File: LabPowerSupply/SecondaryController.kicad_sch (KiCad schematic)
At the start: 18 parts, among them Y2 8M

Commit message: Made oscillator caps smd
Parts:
- C1_Y2, C2_Y2: footprint Capacitor_THT:C_Disc_D5.0mm_W2.5mm_P2.50mm -> (none)
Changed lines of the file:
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@@
     (property "Reference" "C2_Y2" (id 0) (at 73.66 91.44 90))
     (property "Value" "100n" (id 1) (at 73.66 93.98 90))
-    (property "Footprint" "Capacitor_THT:C_Disc_D5.0mm_W2.5mm_P2.50mm" (id 2) (at 77.47 87.3252 0)
+    (property "Footprint" "" (id 2) (at 77.47 87.3252 0)
       (effects (font (size 1.27 1.27)) hide)
     )
@@
     (property "Reference" "C1_Y2" (id 0) (at 73.66 72.39 90))
     (property "Value" "100n" (id 1) (at 73.66 74.93 90))
-    (property "Footprint" "Capacitor_THT:C_Disc_D5.0mm_W2.5mm_P2.50mm" (id 2) (at 77.47 77.7748 0)
-      (effects (font (size 1.27 1.27)) hide)
-    )
+    (property "Footprint" "" (id 2) (at 77.47 77.7748 0)
+      (effects (font (size 1.27 1.27)) hide)
+    )

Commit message: fixed linear cap footprints
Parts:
- C1_Y2, C2_Y2: footprint (none) -> Capacitor_SMD:C_0603_1608Metric
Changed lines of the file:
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@@
     (property "Reference" "C2_Y2" (id 0) (at 73.66 91.44 90))
     (property "Value" "100n" (id 1) (at 73.66 93.98 90))
-    (property "Footprint" "" (id 2) (at 77.47 87.3252 0)
+    (property "Footprint" "Capacitor_SMD:C_0603_1608Metric" (id 2) (at 77.47 87.3252 0)
       (effects (font (size 1.27 1.27)) hide)
     )
@@
     (property "Reference" "C1_Y2" (id 0) (at 73.66 72.39 90))
     (property "Value" "100n" (id 1) (at 73.66 74.93 90))
-    (property "Footprint" "" (id 2) (at 77.47 77.7748 0)
-      (effects (font (size 1.27 1.27)) hide)
-    )
+    (property "Footprint" "Capacitor_SMD:C_0603_1608Metric" (id 2) (at 77.47 77.7748 0)
+      (effects (font (size 1.27 1.27)) hide)
+    )

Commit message: Changed most parts to smd
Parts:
- C1_Power2, C1_Y2, C2_Power2, C2_Y2, C3_Power2, C4_Power2, C5_Power2, C6_Power2, C7_Power2, C8_Power2: footprint Capacitor_SMD:C_0603_1608Metric -> Capacitor_SMD:C_0805_2012Metric
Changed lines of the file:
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@@
     (property "Reference" "C8_Power2" (id 0) (at 116.84 44.45 90))
     (property "Value" "100n" (id 1) (at 116.84 46.99 90))
-    (property "Footprint" "Capacitor_SMD:C_0603_1608Metric" (id 2) (at 120.65 39.6748 0)
+    (property "Footprint" "Capacitor_SMD:C_0805_2012Metric" (id 2) (at 120.65 39.6748 0)
       (effects (font (size 1.27 1.27)) hide)
     )
@@
     (property "Reference" "C2_Y2" (id 0) (at 73.66 91.44 90))
     (property "Value" "100n" (id 1) (at 73.66 93.98 90))
-    (property "Footprint" "Capacitor_SMD:C_0603_1608Metric" (id 2) (at 77.47 87.3252 0)
+    (property "Footprint" "Capacitor_SMD:C_0805_2012Metric" (id 2) (at 77.47 87.3252 0)
       (effects (font (size 1.27 1.27)) hide)
     )
@@
     (property "Reference" "C7_Power2" (id 0) (at 105.41 44.45 90))
     (property "Value" "100n" (id 1) (at 105.41 46.99 90))
-    (property "Footprint" "Capacitor_SMD:C_0603_1608Metric" (id 2) (at 109.22 39.6748 0)
+    (property "Footprint" "Capacitor_SMD:C_0805_2012Metric" (id 2) (at 109.22 39.6748 0)
       (effects (font (size 1.27 1.27)) hide)
     )
@@
     (property "Reference" "C1_Power2" (id 0) (at 82.55 26.67 90))
     (property "Value" "1u" (id 1) (at 82.55 29.21 90))
-    (property "Footprint" "Capacitor_SMD:C_0603_1608Metric" (id 2) (at 86.36 33.3248 0)
+    (property "Footprint" "Capacitor_SMD:C_0805_2012Metric" (id 2) (at 86.36 33.3248 0)
       (effects (font (size 1.27 1.27)) hide)
     )
@@
     (property "Reference" "C5_Power2" (id 0) (at 82.55 44.45 90))
     (property "Value" "100n" (id 1) (at 82.55 46.99 90))
-    (property "Footprint" "Capacitor_SMD:C_0603_1608Metric" (id 2) (at 86.36 39.6748 0)
+    (property "Footprint" "Capacitor_SMD:C_0805_2012Metric" (id 2) (at 86.36 39.6748 0)
       (effects (font (size 1.27 1.27)) hide)
     )
@@
     (property "Reference" "C6_Power2" (id 0) (at 93.98 44.45 90))
     (property "Value" "100n" (id 1) (at 93.98 46.99 90))
-    (property "Footprint" "Capacitor_SMD:C_0603_1608Metric" (id 2) (at 97.79 39.6748 0)
+    (property "Footprint" "Capacitor_SMD:C_0805_2012Metric" (id 2) (at 97.79 39.6748 0)
       (effects (font (size 1.27 1.27)) hide)
     )
@@
     (property "Reference" "C2_Power2" (id 0) (at 93.98 26.67 90))
     (property "Value" "1u" (id 1) (at 93.98 29.21 90))
-    (property "Footprint" "Capacitor_SMD:C_0603_1608Metric" (id 2) (at 97.79 33.3248 0)
+    (property "Footprint" "Capacitor_SMD:C_0805_2012Metric" (id 2) (at 97.79 33.3248 0)
       (effects (font (size 1.27 1.27)) hide)
     )
@@
     (property "Reference" "C1_Y2" (id 0) (at 73.66 72.39 90))
     (property "Value" "100n" (id 1) (at 73.66 74.93 90))
-    (property "Footprint" "Capacitor_SMD:C_0603_1608Metric" (id 2) (at 77.47 77.7748 0)
+    (property "Footprint" "Capacitor_SMD:C_0805_2012Metric" (id 2) (at 77.47 77.7748 0)
       (effects (font (size 1.27 1.27)) hide)
     )
@@
     (property "Reference" "C3_Power2" (id 0) (at 105.41 26.67 90))
     (property "Value" "1u" (id 1) (at 105.41 29.21 90))
-    (property "Footprint" "Capacitor_SMD:C_0603_1608Metric" (id 2) (at 109.22 33.3248 0)
+    (property "Footprint" "Capacitor_SMD:C_0805_2012Metric" (id 2) (at 109.22 33.3248 0)
       (effects (font (size 1.27 1.27)) hide)
     )
@@
     (property "Reference" "C4_Power2" (id 0) (at 116.84 26.67 90))
     (property "Value" "1u" (id 1) (at 116.84 29.21 90))
-    (property "Footprint" "Capacitor_SMD:C_0603_1608Metric" (id 2) (at 120.65 33.3248 0)
-      (effects (font (size 1.27 1.27)) hide)
-    )
+    (property "Footprint" "Capacitor_SMD:C_0805_2012Metric" (id 2) (at 120.65 33.3248 0)
+      (effects (font (size 1.27 1.27)) hide)
+    )

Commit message: Fixed oscillator caps, began changing resistors to more common values
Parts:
- C1_Y2, C2_Y2: value 100n -> 20p; footprint Capacitor_SMD:C_0805_2012Metric -> Capacitor_SMD:C_0603_1608Metric
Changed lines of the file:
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@@
     (in_bom yes) (on_board yes)
     (property "Reference" "C2_Y2" (id 0) (at 73.66 91.44 90))
-    (property "Value" "100n" (id 1) (at 73.66 93.98 90))
-    (property "Footprint" "Capacitor_SMD:C_0805_2012Metric" (id 2) (at 77.47 87.3252 0)
+    (property "Value" "20p" (id 1) (at 73.66 93.98 90))
+    (property "Footprint" "Capacitor_SMD:C_0603_1608Metric" (id 2) (at 77.47 87.3252 0)
       (effects (font (size 1.27 1.27)) hide)
     )
@@
     (in_bom yes) (on_board yes)
     (property "Reference" "C1_Y2" (id 0) (at 73.66 72.39 90))
-    (property "Value" "100n" (id 1) (at 73.66 74.93 90))
-    (property "Footprint" "Capacitor_SMD:C_0805_2012Metric" (id 2) (at 77.47 77.7748 0)
-      (effects (font (size 1.27 1.27)) hide)
-    )
+    (property "Value" "20p" (id 1) (at 73.66 74.93 90))
+    (property "Footprint" "Capacitor_SMD:C_0603_1608Metric" (id 2) (at 77.47 77.7748 0)
+      (effects (font (size 1.27 1.27)) hide)
+    )

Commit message: almost done
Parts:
- removed J_STLink2: Conn_01x03_Male, Connector_PinHeader_2.54mm:PinHeader_1x03_P2.54mm_Vertical, symbol Connector:Conn_01x03_Male
- added J_STLink2: Conn_01x03_Male, Connector_PinHeader_2.54mm:PinHeader_1x03_P2.54mm_Vertical, symbol Connector:Conn_01x05_Male
- C1_Power2, C2_Power2, C3_Power2, C4_Power2, C5_Power2, C6_Power2, C7_Power2, C8_Power2: footprint Capacitor_SMD:C_0805_2012Metric -> Capacitor_SMD:C_0603_1608Metric
- renumbered R2_Boot2 to R1_Boot2, R1_Boot2 to R2_Boot2
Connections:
- net 3.3 Volts: now also J_STLink2.1 (Pin_1)
- net GND: now also J_STLink2.2 (Pin_2)
- net at MCU_2.34 (PA13): now also J_STLink2.3 (Pin_3)
- net at MCU_2.37 (PA14): now also J_STLink2.4 (Pin_4)
- net at MCU_2.7 (NRST), R_Reset2.2, SW_Reset2.3 (B)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: now also J_STLink2.5 (Pin_5)
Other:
- moved on the sheet: SW_Reset2

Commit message: SMD Oscillator
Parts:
- Y2: footprint Crystal:Crystal_HC18-U_Vertical -> Crystal:Crystal_SMD_HC49-SD
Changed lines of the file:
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@@
       (effects (font (size 1.27 1.27)) (justify right))
     )
-    (property "Footprint" "Crystal:Crystal_HC18-U_Vertical" (id 2) (at 77.47 82.55 0)
+    (property "Footprint" "Crystal:Crystal_SMD_HC49-SD" (id 2) (at 77.47 82.55 0)
       (effects (font (size 1.27 1.27)) hide)
     )

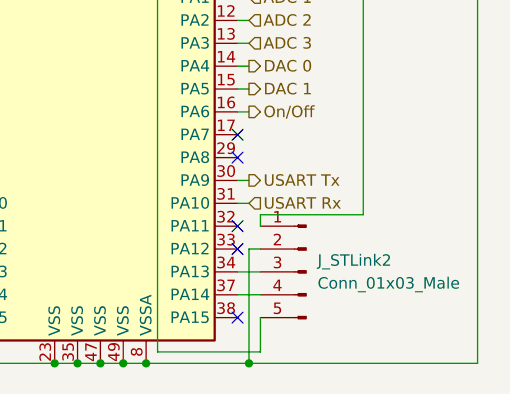
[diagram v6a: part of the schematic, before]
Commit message: removed transformer and bug squached
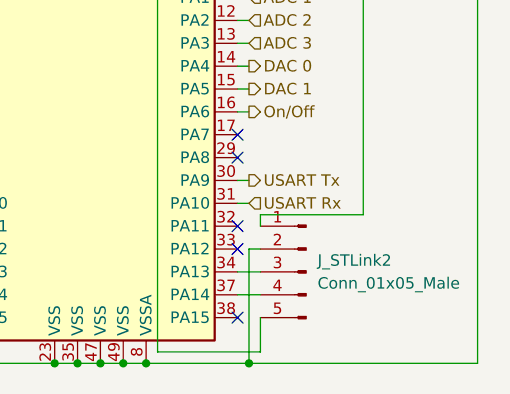
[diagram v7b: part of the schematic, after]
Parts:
- J_STLink2: value Conn_01x03_Male -> Conn_01x05_Male; footprint Connector_PinHeader_2.54mm:PinHeader_1x03_P2.54mm_Vertical -> Connector_PinHeader_2.54mm:PinHeader_1x05_P2.54mm_Vertical
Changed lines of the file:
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@@
       (effects (font (size 1.27 1.27)) (justify right))
     )
-    (property "Value" "Conn_01x03_Male" (id 1) (at 124.46 130.8099 0)
+    (property "Value" "Conn_01x05_Male" (id 1) (at 124.46 130.8099 0)
       (effects (font (size 1.27 1.27)) (justify right))
     )
-    (property "Footprint" "Connector_PinHeader_2.54mm:PinHeader_1x03_P2.54mm_Vertical" (id 2) (at 123.19 129.54 0)
+    (property "Footprint" "Connector_PinHeader_2.54mm:PinHeader_1x05_P2.54mm_Vertical" (id 2) (at 123.19 129.54 0)
       (effects (font (size 1.27 1.27)) hide)
     )

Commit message: routing is weird
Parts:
- SW_Reset2: footprint Button_Switch_SMD:SW_MEC_5GSH9 -> Button_Switch_THT:SW_PUSH-12mm
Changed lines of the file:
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@@
       (effects (font (size 1.27 1.27)) (justify right))
     )
-    (property "Footprint" "Button_Switch_SMD:SW_MEC_5GSH9" (id 2) (at 63.5 68.58 0)
+    (property "Footprint" "Button_Switch_THT:SW_PUSH-12mm" (id 2) (at 63.5 68.58 0)
       (effects (font (size 1.27 1.27)) hide)
     )
